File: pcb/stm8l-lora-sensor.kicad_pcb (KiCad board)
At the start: 2 copper layers, 35 parts, among them J1 Conn_01x06, J2 Conn_01x02, J3 Conn_01x03, J4 Conn_01x03, J5 Conn_01x02, J6 Conn_01x02, U1 74HC595, U2 STM8L051F3P, U3 74HC595, U4 CA56-12EWA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

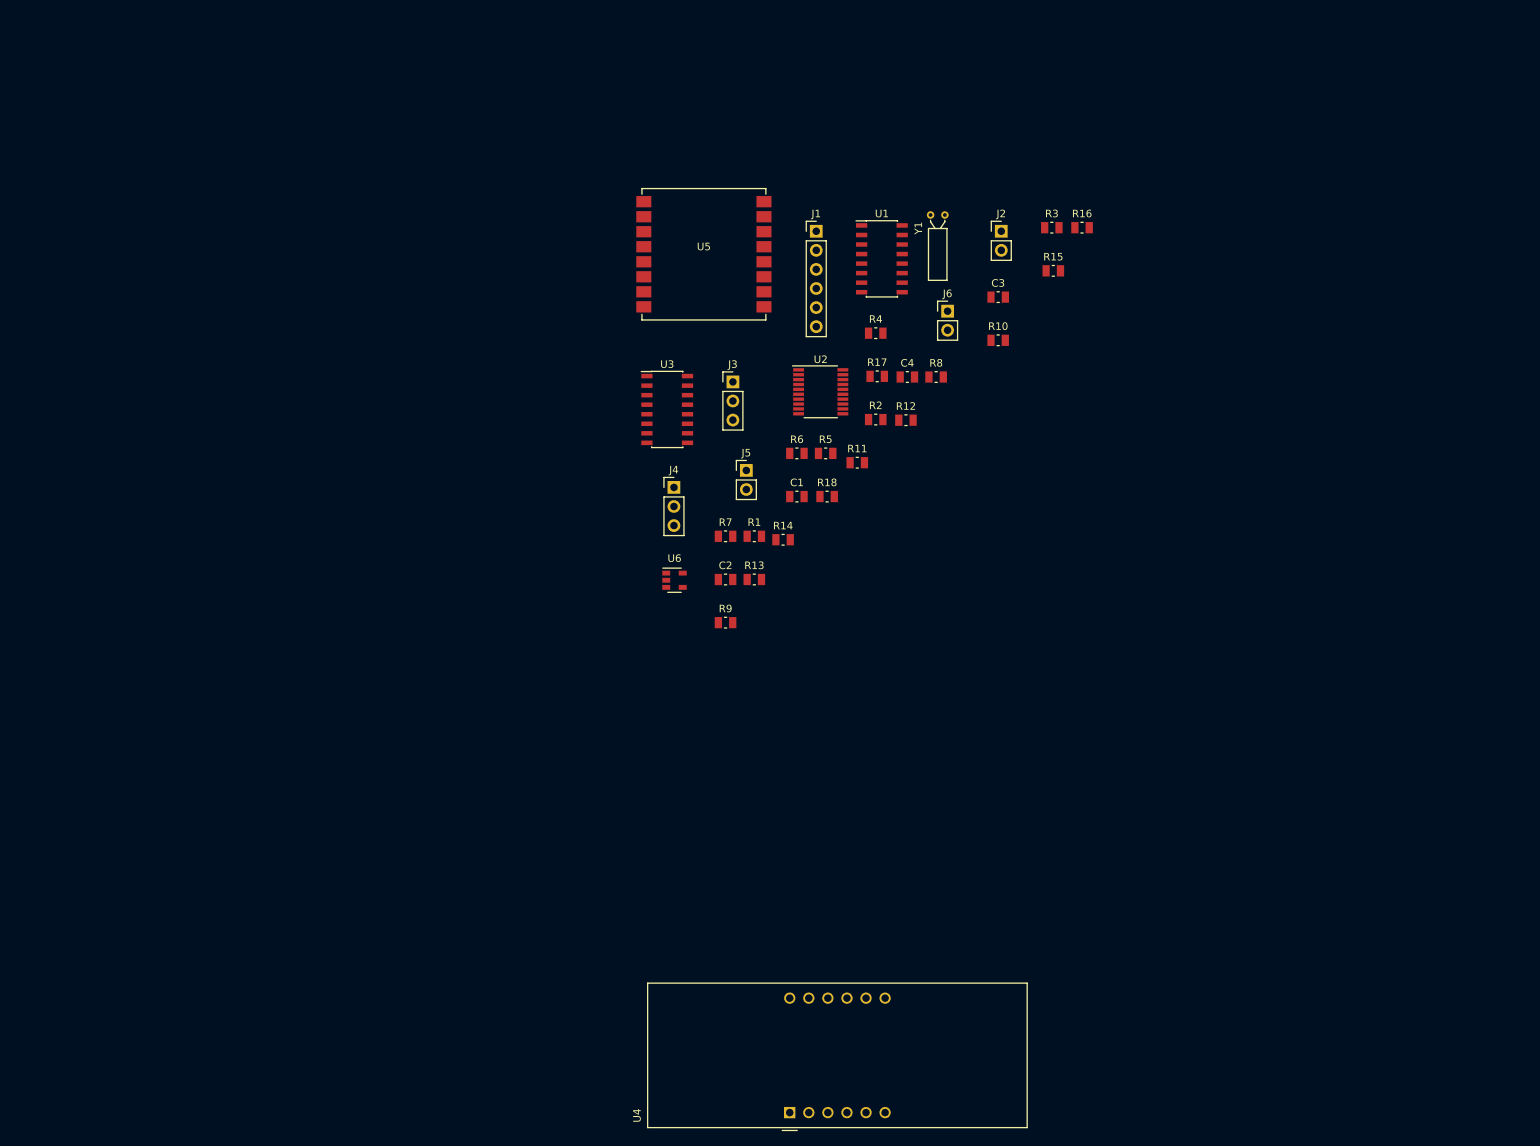
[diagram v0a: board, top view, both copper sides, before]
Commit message: sensor back on i2c
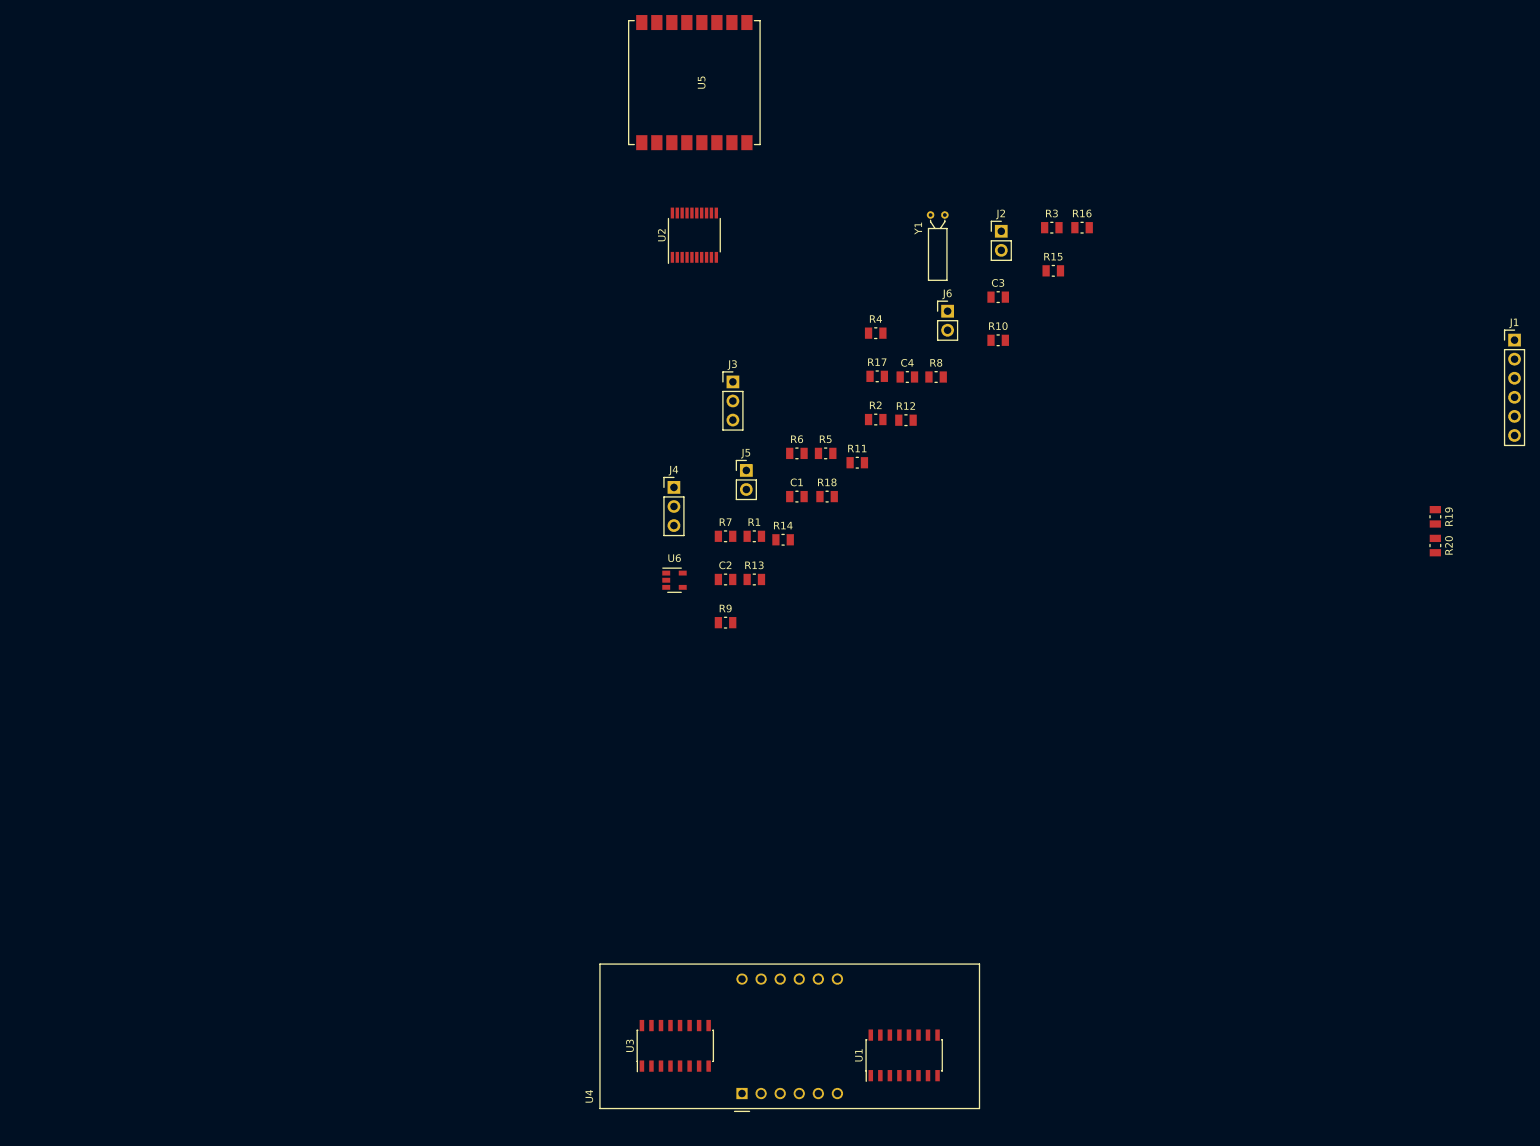
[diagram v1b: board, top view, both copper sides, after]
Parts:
- added R19: 10k, Resistor_SMD:R_0805_2012Metric, F.Cu at (207.9, 85.8)
- added R20: 10k, Resistor_SMD:R_0805_2012Metric, F.Cu at (207.9, 89.6)
- moved U1 106.1 mm to (137.2, 157.5), turned to 90 degrees
- moved J1 94.1 mm to (218.4, 62.2)
- moved U3 84.7 mm to (106.7, 156.2), turned to 90 degrees
- moved U2 26.8 mm to (109.2, 48.3), turned to 90 degrees
- moved U5 22.9 mm to (109.2, 27.9), turned to 270 degrees
- moved U4 6.84 mm to (115.6, 162.6)
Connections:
- J1 pad 3: SPI1_SCK -> SCL
- J1 pad 4: SPI1_MOSI -> SDA
- J1 pad 5: CS_SENSOR -> VCC
- J1 pad 6: SPI1_MISO -> GND
- U2 pad 14: Net-(U2-Pad14) -> CS_LORA
- U2 pad 18: CS_LORA -> SDA
- U2 pad 19: CS_SENSOR -> SCL

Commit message: pcb placement done. Have to change LED indicator
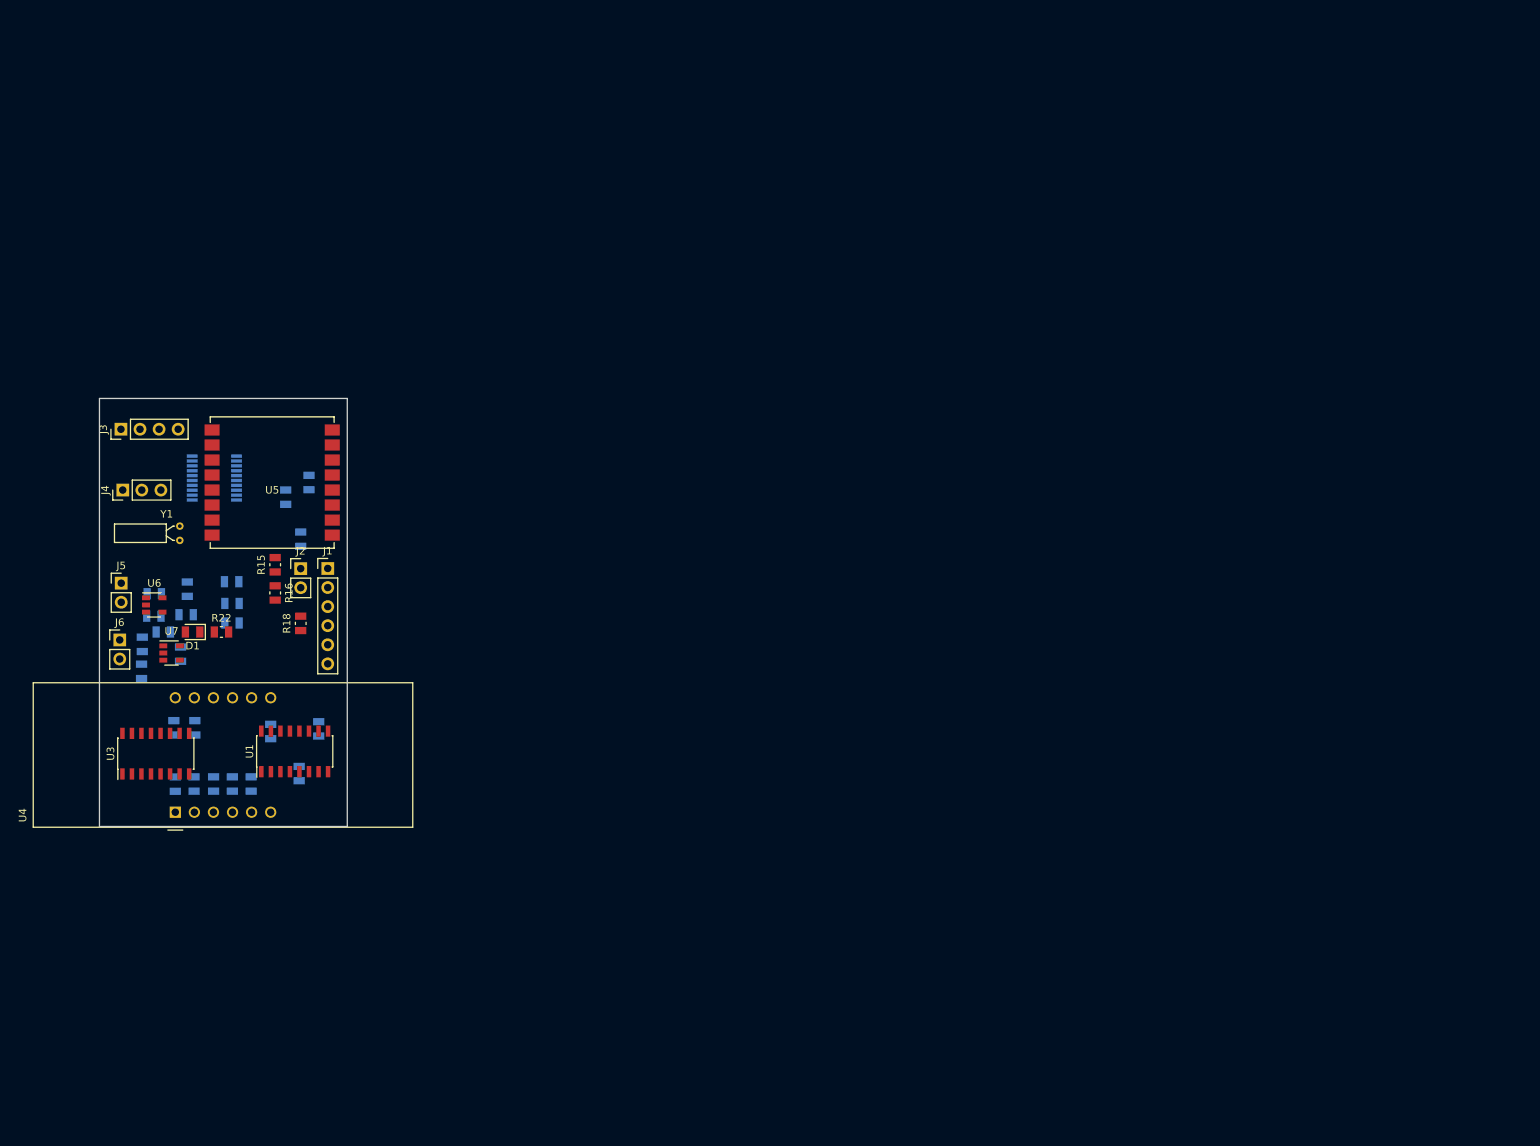
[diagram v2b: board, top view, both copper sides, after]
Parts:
- added C5: 4.7u, Capacitor_SMD:C_0805_2012Metric, B.Cu at (38.5, 101.1)
- added C6: 1u, Capacitor_SMD:C_0805_2012Metric, B.Cu at (40.8, 104.0)
- added D1: LED, LED_SMD:LED_0805_2012Metric, F.Cu at (42.4, 101.1)
- added R21: 10k, Resistor_SMD:R_0805_2012Metric, B.Cu at (41.7, 95.4)
- added R22: 470, Resistor_SMD:R_0805_2012Metric, F.Cu at (46.2, 101.1)
- added U7: LP2985-3.3, Package_TO_SOT_SMD:SOT-23-5, F.Cu at (39.6, 103.9)
- C1, C3, C4, R13, R14, R17, R19, R6, R7, R8, R9, U2: moved to B.Cu
- C2: value 1u -> 4.7u; moved to B.Cu
- J3: value Conn_01x03 -> Conn_01x04; footprint Connector_PinHeader_2.54mm:PinHeader_1x03_P2.54mm_Vertical -> Connector_PinHeader_2.54mm:PinHeader_1x04_P2.54mm_Vertical
- R1: value 10k -> 100k; moved to B.Cu
- R10, R11: value 10k -> 1k; moved to B.Cu
- R12: value 100k -> 1k; moved to B.Cu
- R15, R16: value 100k -> 10k
- R18: value 100k -> 1k
- R2, R4, R5: value 1k -> 100k; moved to B.Cu
- R20: value 10k -> 2k; moved to B.Cu
- R3: value 1k -> 10k; moved to B.Cu
- U6: value LP2985-3.3 -> MCP73831-2-OT
- moved R20 170.7 mm to (37.3, 96.0), turned to 0 degrees
- moved J1 160.9 mm to (60.4, 92.6)
- moved R19 153.1 mm to (54.8, 83.1)
- moved R10 124.5 mm to (40.1, 121.4), turned to 90 degrees
- moved J6 118.6 mm to (32.7, 102.2)
- moved R3 118.3 mm to (59.2, 114.0), turned to 90 degrees
- moved R16 117.9 mm to (53.4, 95.9), turned to 270 degrees
- moved R15 110.8 mm to (53.4, 92.1), turned to 90 degrees
- moved C4 109.3 mm to (35.6, 106.3), turned to 270 degrees
- moved C3 108.9 mm to (47.6, 94.4)
- moved R8 108.3 mm to (47.7, 121.3), turned to 270 degrees
- moved Y1 108.2 mm to (40.7, 87.0), turned to 270 degrees
- moved J2 103.5 mm to (56.8, 92.7)
- moved R12 99.8 mm to (50.2, 121.3), turned to 270 degrees
- moved R4 99.2 mm to (41.5, 98.8)
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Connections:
- C4 pad 1: VCC -> +BATT
- J3 pad 1: DRX -> VCC
- J3 pad 2: DTX -> SWIM
- J3 pad 3: GND -> RST
- J4 pad 1: SWIM -> DRX
- J4 pad 2: RST -> DTX
- J6 pad 1: Net-(J6-Pad1) -> +BATT
- J6 pad 2: Net-(J6-Pad2) -> GND
- R1 pad 1: VCC -> +BATT
- R1 pad 2: Net-(R1-Pad2) -> ADC_LIPO
- R10 pad 1: VCC -> Net-(R10-Pad1)
- R11 pad 1: Net-(C1-Pad1) -> Net-(R11-Pad1)
- R11 pad 2: VCC -> Net-(R11-Pad2)
- R12 pad 1: BTN -> Net-(R12-Pad1)
- R12 pad 2: VCC -> Net-(R12-Pad2)
- R13 pad 1: GND -> Net-(R13-Pad1)
- R13 pad 2: Net-(J2-Pad2) -> Net-(R13-Pad2)
- R14 pad 1: RST -> VCC
- R14 pad 2: VCC -> Net-(R14-Pad2)
- R15 pad 1: Net-(J6-Pad1) -> SCL
- R15 pad 2: ADC_LIPO -> VCC
- R16 pad 1: ADC_LIPO -> SDA
- R16 pad 2: GND -> VCC
- R17 pad 1: Net-(J6-Pad2) -> BTN
- R17 pad 2: ADC_SOLAR -> VCC
- R18 pad 1: ADC_SOLAR -> GND
- R18 pad 2: GND -> Net-(J2-Pad2)
- R19 pad 1: SCL -> Net-(C1-Pad1)
- R2 pad 1: Net-(R2-Pad1) -> ADC_LIPO
- R2 pad 2: Net-(R2-Pad2) -> GND
- R20 pad 1: SDA -> GND
- R20 pad 2: VCC -> Net-(R20-Pad2)
- R3 pad 1: Net-(R3-Pad1) -> VCC
- R4 pad 1: Net-(R4-Pad1) -> +5V
- R4 pad 2: Net-(R4-Pad2) -> ADC_SOLAR
- R5 pad 1: Net-(R5-Pad1) -> ADC_SOLAR
- R5 pad 2: Net-(R5-Pad2) -> GND
- U1 pad 1: Net-(R3-Pad1) -> Net-(R7-Pad1)
- U1 pad 10: Net-(R1-Pad2) -> Net-(R3-Pad2)
- U1 pad 15: Net-(R2-Pad1) -> Net-(R6-Pad1)
- U1 pad 2: Net-(R4-Pad1) -> Net-(R8-Pad1)
- U1 pad 3: Net-(R5-Pad1) -> Net-(R9-Pad1)
- U1 pad 4: Net-(R6-Pad1) -> Net-(R10-Pad1)
- U1 pad 5: Net-(R7-Pad1) -> Net-(R11-Pad1)
- U1 pad 6: Net-(R8-Pad1) -> Net-(R12-Pad1)
- U1 pad 7: Net-(R9-Pad1) -> Net-(R13-Pad1)
- U3 pad 10: Net-(R10-Pad2) -> Net-(R14-Pad2)
- U4 pad 1: Net-(R6-Pad2) -> Net-(R10-Pad2)
- U4 pad 10: Net-(R7-Pad2) -> Net-(R11-Pad2)
- U4 pad 11: Net-(R2-Pad2) -> Net-(R6-Pad2)
- U4 pad 2: Net-(R5-Pad2) -> Net-(R9-Pad2)
- U4 pad 3: Net-(R9-Pad2) -> Net-(R13-Pad2)
- U4 pad 4: Net-(R4-Pad2) -> Net-(R8-Pad2)
- U4 pad 5: Net-(R8-Pad2) -> Net-(R12-Pad2)
- U4 pad 7: Net-(R3-Pad2) -> Net-(R7-Pad2)
- U6 pad 1: +5V -> Net-(R22-Pad2)
- U6 pad 3: +5V -> +BATT
- U6 pad 4: Net-(U6-Pad4) -> +5V
- U6 pad 5: VCC -> Net-(R20-Pad2)
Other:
- board outline added: 33 x 57 mm

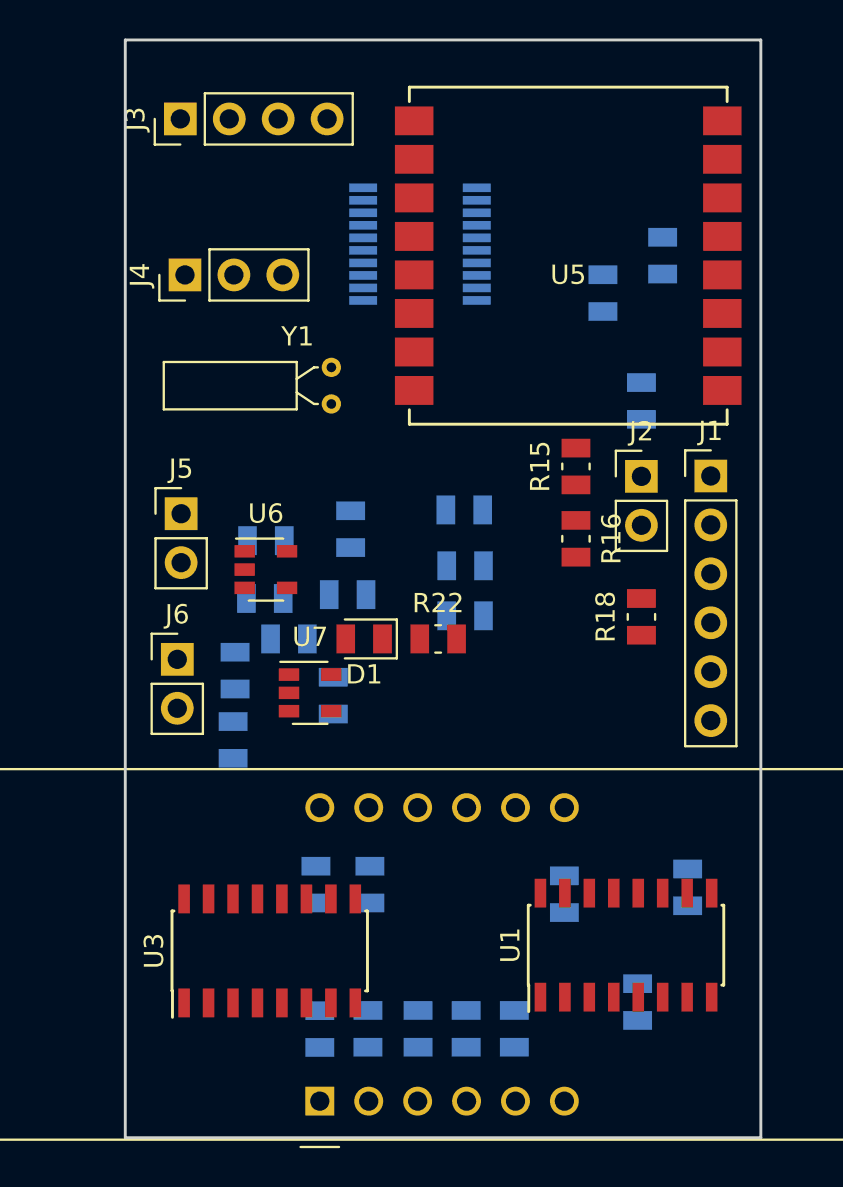
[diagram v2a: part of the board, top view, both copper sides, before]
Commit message: Added bypass caps, started pcb
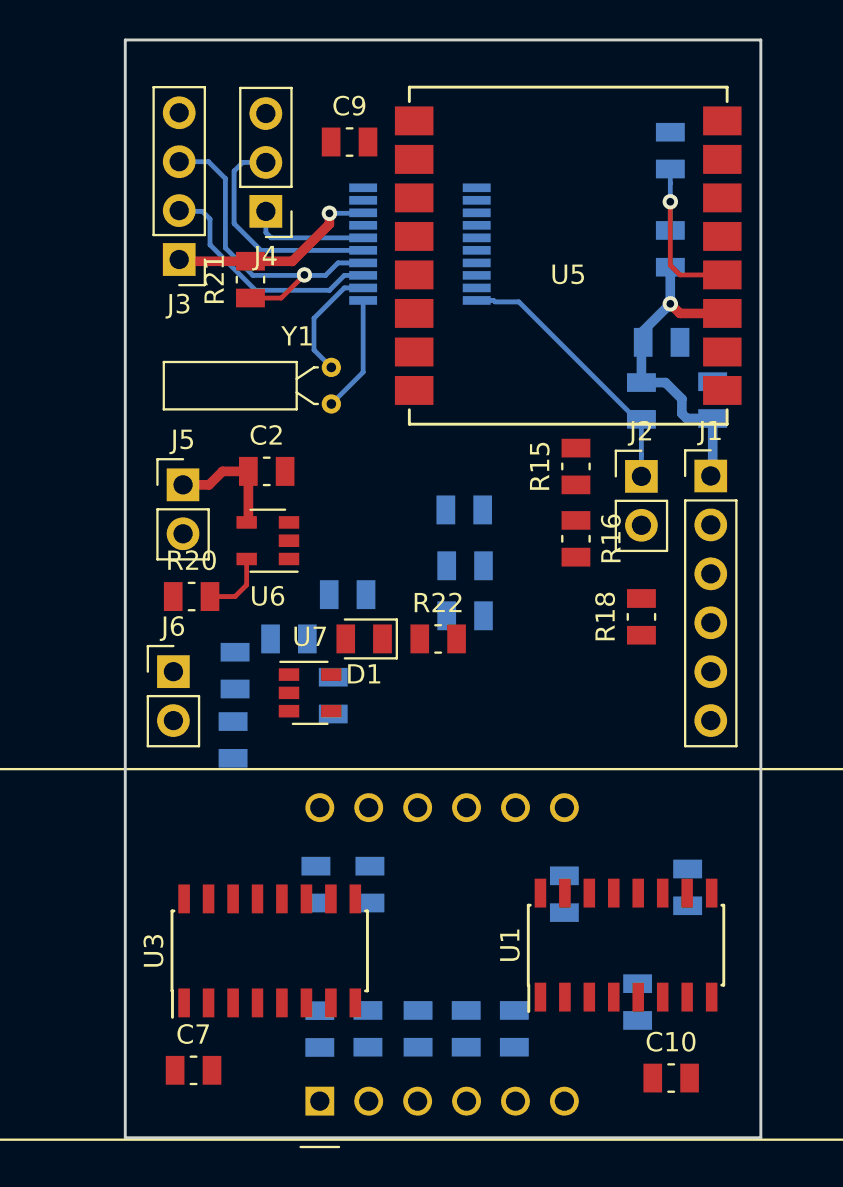
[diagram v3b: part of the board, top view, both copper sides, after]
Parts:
- added C10: 0.1u, Capacitor_SMD:C_0805_2012Metric, F.Cu at (58.3, 123.9)
- added C11: 0.1u, Capacitor_SMD:C_0805_2012Metric, B.Cu at (57.8, 85.7)
- added C7: 0.1u, Capacitor_SMD:C_0805_2012Metric, F.Cu at (33.5, 123.5)
- added C8: 0.1u, Capacitor_SMD:C_0805_2012Metric, B.Cu at (60.5, 88.7)
- added C9: 0.1u, Capacitor_SMD:C_0805_2012Metric, F.Cu at (41.6, 75.3)
- C2, R21: moved to F.Cu
- R20: value 2k -> 10k; moved to F.Cu
- moved R21 14.0 mm to (36.5, 82.4), turned to 90 degrees
- moved J3 7.30 mm to (32.8, 81.4), turned to 180 degrees
- moved C2 6.60 mm to (37.3, 92.4), turned to 0 degrees
- moved C1 5.47 mm to (58.3, 75.7)
- moved J4 5.34 mm to (37.3, 78.9), turned to 180 degrees
- moved R20 4.82 mm to (33.4, 98.9)
- moved R19 4.19 mm to (58.3, 80.8)
- moved J5 1.50 mm to (33.0, 93.1)
- moved U6 1.50 mm to (37.4, 96.0), turned to 180 degrees
- moved J6 0.67 mm to (32.5, 102.8)
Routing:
- net VCC: track 0.00 -> 28.6 mm, vias 0 -> 2
- net RST: track 0.00 -> 17.7 mm, vias 0 -> 1
- net BTN: track 0.00 -> 14.1 mm
- net SWIM: track 0.00 -> 12.4 mm
- net DTX: track 0.00 -> 11.8 mm
- net Net-(C1-Pad1): track 0.00 -> 9.40 mm, vias 0 -> 1
- net +5V: track 0.00 -> 6.37 mm
- net DRX: track 0.00 -> 6.26 mm
- net Net-(U2-Pad2): track 0.00 -> 6.13 mm
- net Net-(U2-Pad1): track 0.00 -> 6.06 mm
- net Net-(R20-Pad2): track 0.00 -> 3.50 mm
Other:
- net class Power added: clearance 0.2, trace_width 0.5, via_dia 0.8, via_drill 0.4

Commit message: more pcb
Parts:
- C3, C4, C5, C6, R1, R2, R4, R5: moved to F.Cu
- moved C3 18.4 mm to (32.9, 83.3), turned to 180 degrees
- moved D1 14.2 mm to (33.8, 89.8)
- moved R22 14.1 mm to (37.8, 89.8)
- moved C5 7.41 mm to (40.8, 94.1), turned to 90 degrees
- moved R15 7.32 mm to (56.7, 98.7), turned to 180 degrees
- moved R18 6.56 mm to (53.4, 94.3), turned to 270 degrees
- moved R16 6.30 mm to (56.6, 101.3), turned to 180 degrees
- moved R2 6.02 mm to (42.9, 101.0)
- moved C6 5.30 mm to (46.1, 103.9)
- moved R5 5.11 mm to (42.9, 97.9)
- moved R4 2.85 mm to (38.7, 98.9)
- moved U7 2.80 mm to (42.4, 104.0)
- moved C4 2.12 mm to (37.5, 105.4), turned to 0 degrees
- moved R1 1.91 mm to (37.5, 102.1), turned to 0 degrees
- moved Y1 1.84 mm to (40.0, 85.3)
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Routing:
- net VCC: track 28.6 -> 89.1 mm, vias 2 -> 3
- net IND_LATCH: track 0.00 -> 34.7 mm
- net IND_DATA: track 0.00 -> 31.8 mm
- net SDA: track 0.00 -> 31.1 mm, vias 0 -> 1
- net IND_CLK: track 0.00 -> 31.0 mm
- net ADC_LIPO: track 0.00 -> 29.4 mm, vias 0 -> 1
- net SCL: track 0.00 -> 26.6 mm, vias 0 -> 1
- net +BATT: track 0.00 -> 26.4 mm, vias 0 -> 2
- net ADC_SOLAR: track 0.00 -> 25.5 mm, vias 0 -> 1
- net +5V: track 6.37 -> 26.0 mm
- net CS_LORA: track 0.00 -> 16.9 mm, vias 0 -> 1
- net SPI1_MOSI: track 0.00 -> 12.0 mm, vias 0 -> 1
- net SPI1_SCK: track 0.00 -> 9.88 mm, vias 0 -> 1
- net Net-(R22-Pad2): track 0.00 -> 8.61 mm
- net SPI1_MISO: track 0.00 -> 8.46 mm, vias 0 -> 1
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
